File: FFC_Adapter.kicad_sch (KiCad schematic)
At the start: 20 parts, among them J1 LIF_16

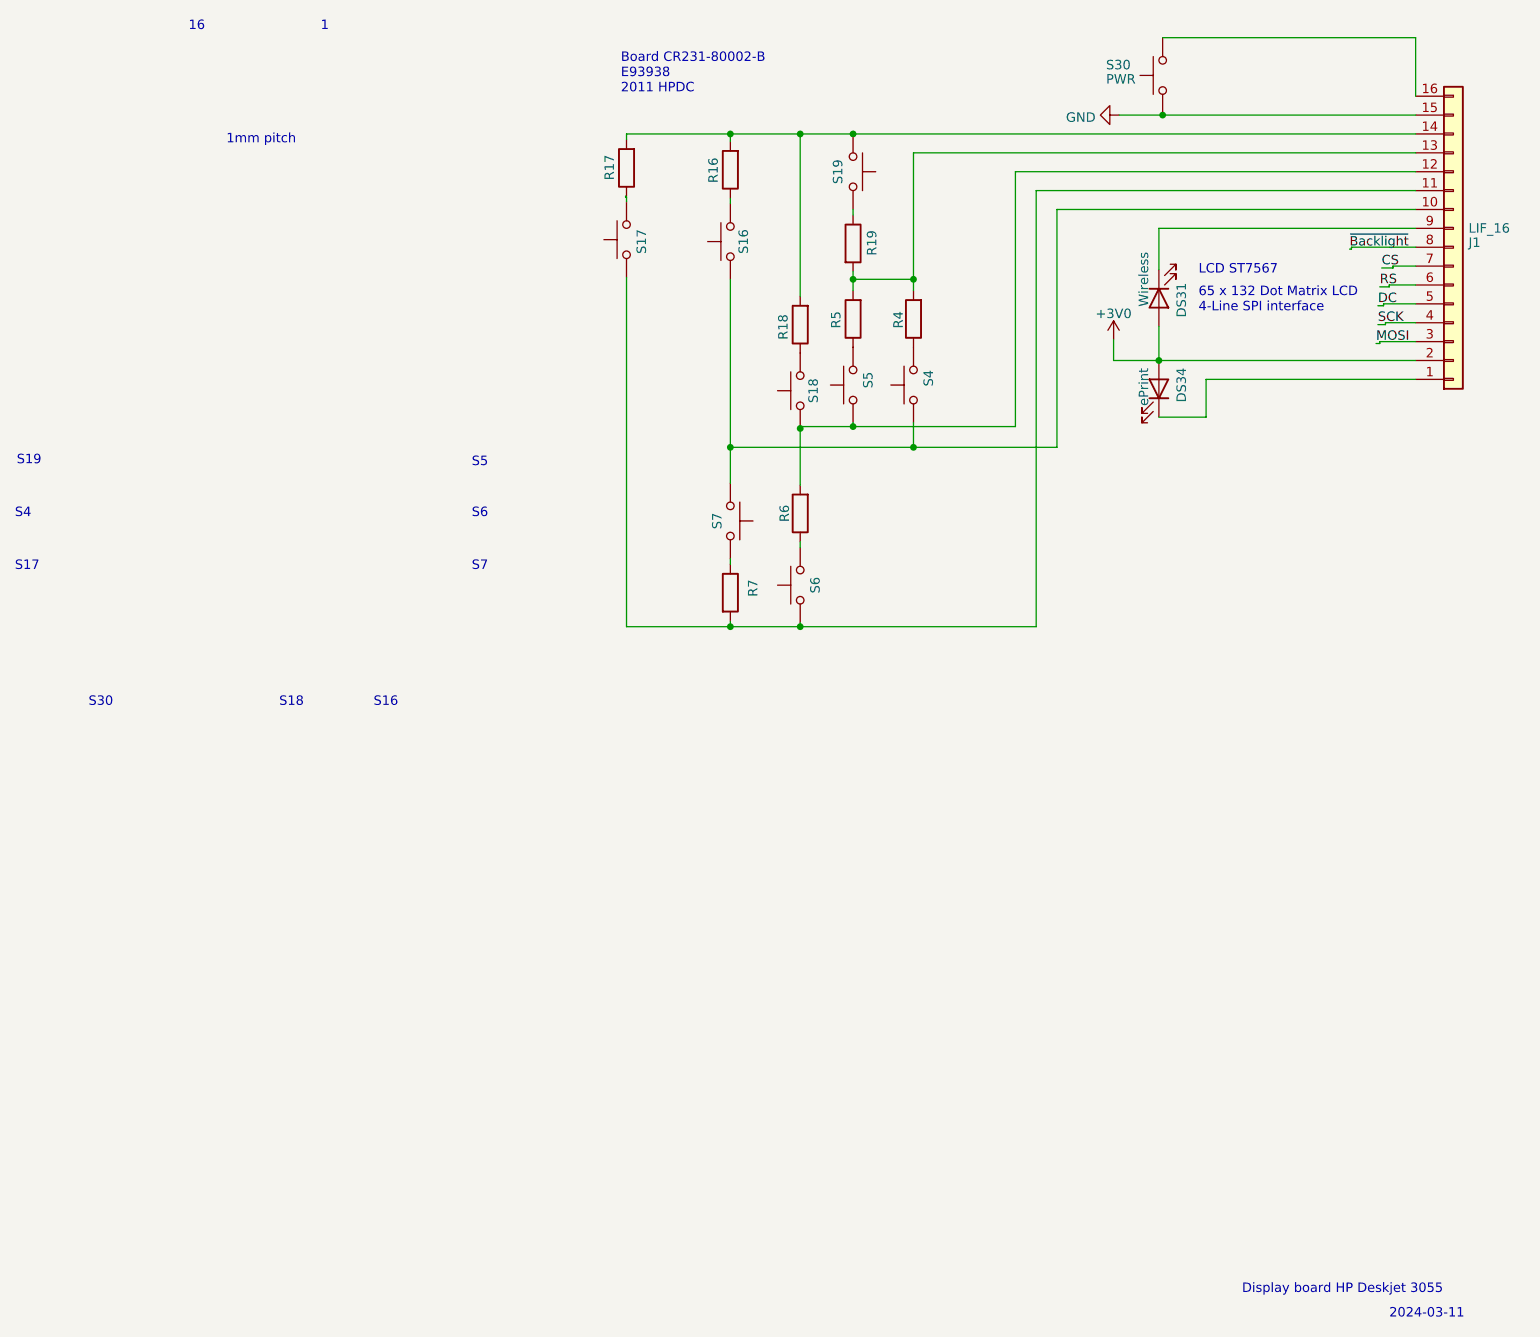
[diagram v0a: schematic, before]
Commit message: + LIF connector view + LCD Type
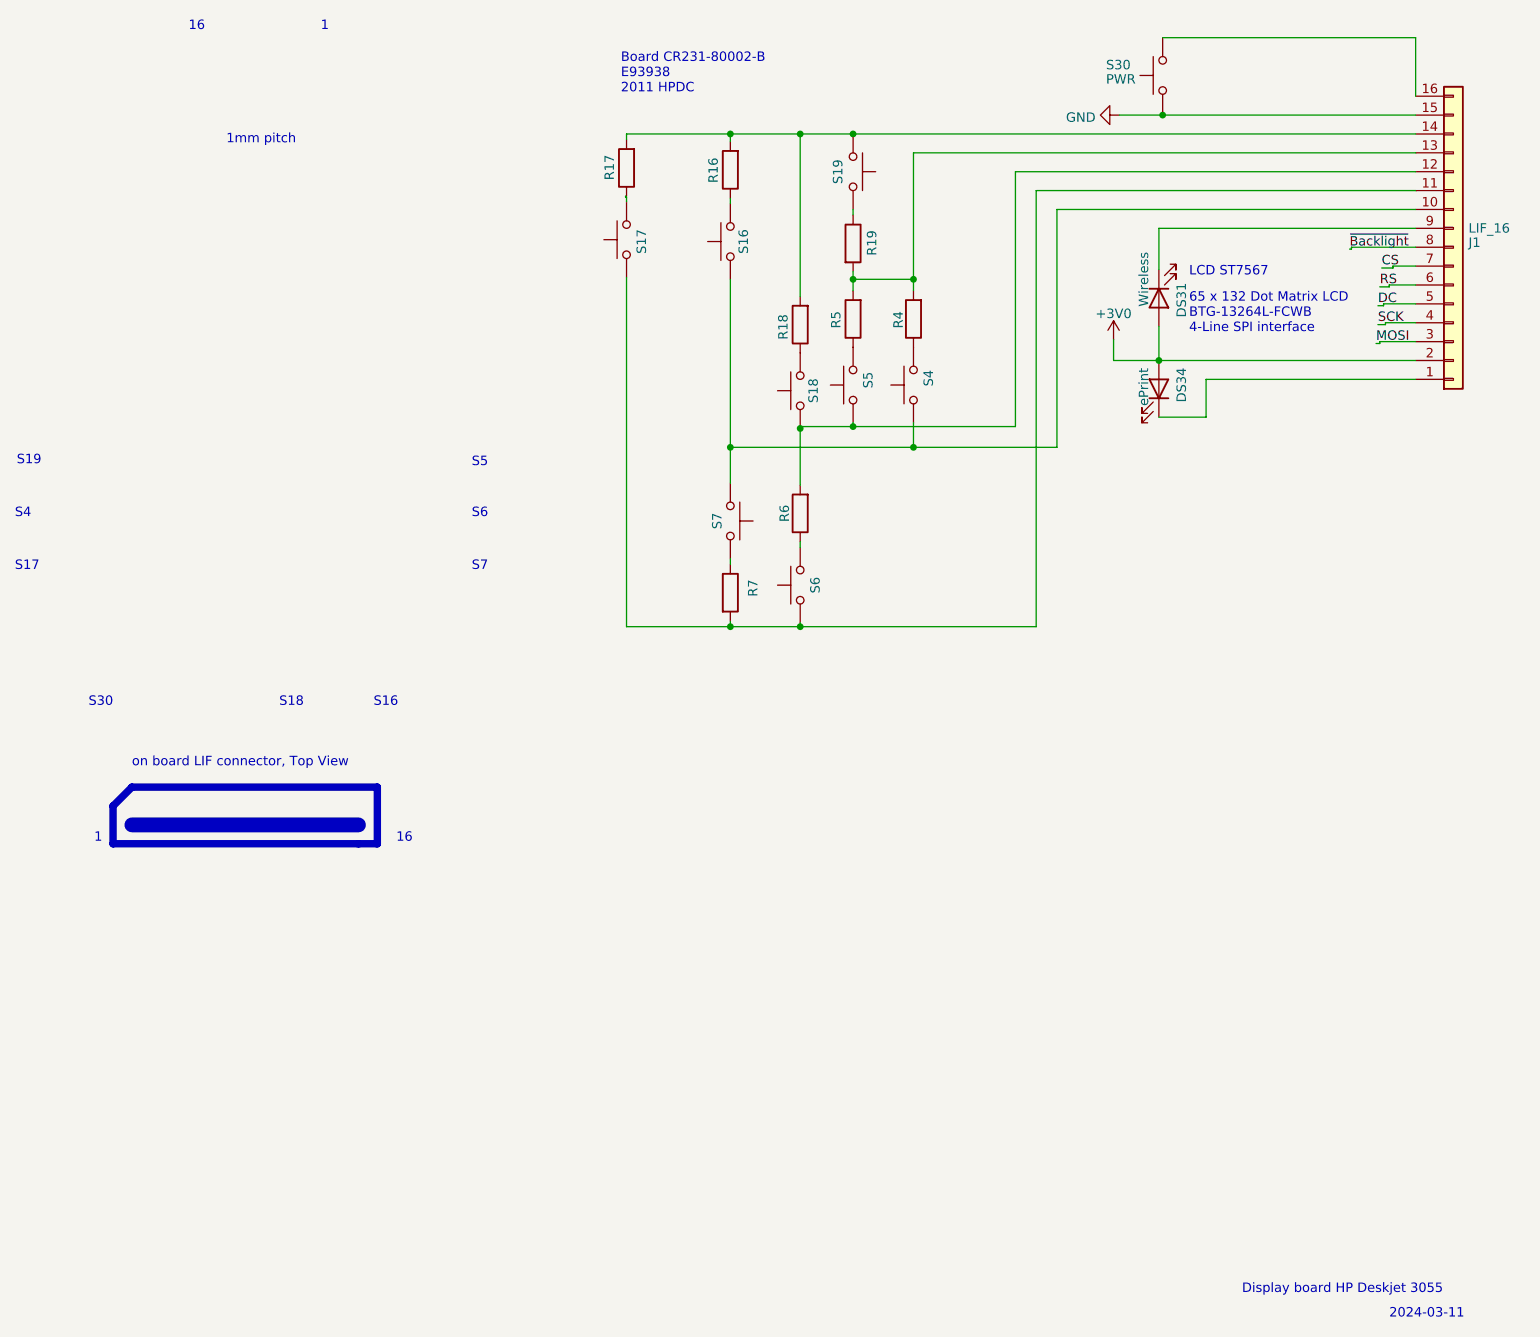
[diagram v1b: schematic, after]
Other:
- note added: "65 x 132 Dot Matrix LCD BTG-13264L-FCWB 4-Line SPI interface"
- note added: "on board LIF connector, Top View"
- note removed: "65 x 132 Dot Matrix LCD 4-Line SPI interface"
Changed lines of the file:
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@@
     (stroke (width 0) (type default))
   )
+  (polyline (pts (xy 38.1 129.54) (xy 38.1 124.46))
+    (stroke (width 1) (type default) (color 72 72 72 1))
+  )
   (wire (pts (xy 137.668 73.406) (xy 159.512 73.406))
     (stroke (width 0) (type default))
@@
     (stroke (width 0) (type default))
   )
+  (polyline (pts (xy 71.12 129.54) (xy 38.1 129.54))
+    (stroke (width 1) (type default) (color 72 72 72 1))
+  )
   (wire (pts (xy 107.061 42.545) (xy 107.061 42.418))
     (stroke (width 0) (type default))
@@
     (stroke (width 0) (type default))
   )
+  (polyline (pts (xy 73.66 121.92) (xy 73.66 129.54))
+    (stroke (width 1) (type default) (color 72 72 72 1))
+  )
   (wire (pts (xy 121.158 99.568) (xy 121.158 100.33))
     (stroke (width 0) (type default))
@@
     (stroke (width 0) (type default))
   )
+  (polyline (pts (xy 40.64 127) (xy 71.12 127))
+    (stroke (width 2) (type default) (color 0 0 0 1))
+  )
   (wire (pts (xy 121.158 34.036) (xy 121.158 35.052))
     (stroke (width 0) (type default))
@@
     (stroke (width 0) (type default))
   )
+  (polyline (pts (xy 71.12 129.54) (xy 73.66 129.54))
+    (stroke (width 1) (type default) (color 72 72 72 1))
+  )
   (wire (pts (xy 209.296 59.69) (xy 209.296 59.436))
     (stroke (width 0) (type default))
   )
+  (polyline (pts (xy 38.1 124.46) (xy 40.64 121.92))
+    (stroke (width 1) (type default) (color 72 72 72 1))
+  )
   (wire (pts (xy 210.312 51.816) (xy 213.36 51.816))
     (stroke (width 0) (type default))
@@
     (stroke (width 0) (type default))
   )
+  (polyline (pts (xy 40.64 121.92) (xy 73.66 121.92))
+    (stroke (width 1) (type default) (color 72 72 72 1))
+  )
   (wire (pts (xy 121.158 34.036) (xy 130.556 34.036))
     (stroke (width 0) (type default))
@@
     (effects (font (size 1.27 1.27)) (justify left bottom))
   )
+  (text "on board LIF connector, Top View" (at 40.64 119.38 0)
+    (effects (font (size 1.27 1.27)) (justify left bottom))
+  )
   (text "S6" (at 86.36 85.852 0)
     (effects (font (size 1.27 1.27)) (justify left bottom))
@@
     (effects (font (size 1.27 1.27)) (justify left bottom))
   )
-  (text "65 x 132 Dot Matrix LCD\n4-Line SPI interface" (at 184.15 58.166 0)
+  (text "65 x 132 Dot Matrix LCD\nBTG-13264L-FCWB\n4-Line SPI interface"
+    (at 182.88 60.96 0)
     (effects (font (size 1.27 1.27)) (justify left bottom))
   )
@@
     (effects (font (size 1.27 1.27)) (justify left bottom))
   )
+  (text "1" (at 35.56 129.54 0)
+    (effects (font (size 1.27 1.27)) (justify left bottom))
+  )
   (text "16" (at 48.26 20.32 0)
     (effects (font (size 1.27 1.27)) (justify left bottom))
@@
     (effects (font (size 1.27 1.27)) (justify left bottom))
   )
-  (text "LCD ST7567" (at 184.15 53.086 0)
+  (text "16" (at 76.2 129.54 0)
+    (effects (font (size 1.27 1.27)) (justify left bottom))
+  )
+  (text "LCD ST7567" (at 182.88 53.34 0)
     (effects (font (size 1.27 1.27)) (justify left bottom))
   )
